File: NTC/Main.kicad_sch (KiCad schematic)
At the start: 37 parts, among them U1 TDN_5-0911WISM, X1 Barrel_Jack_Switch, X2.1 Conn_01x01_Pin, X2.2 Conn_01x01_Pin, X21 Conn_01x04_Socket, X3.1 Conn_01x01_Pin, X3.2 Conn_01x01_Pin, X4.1 Conn_01x01_Pin, X4.2 Conn_01x01_Pin, X4.3 Conn_01x01_Pin, X5.1 Conn_01x01_Pin, X5.2 Conn_01x01_Pin, X6 Conn_02x20_Counter_Clockwise

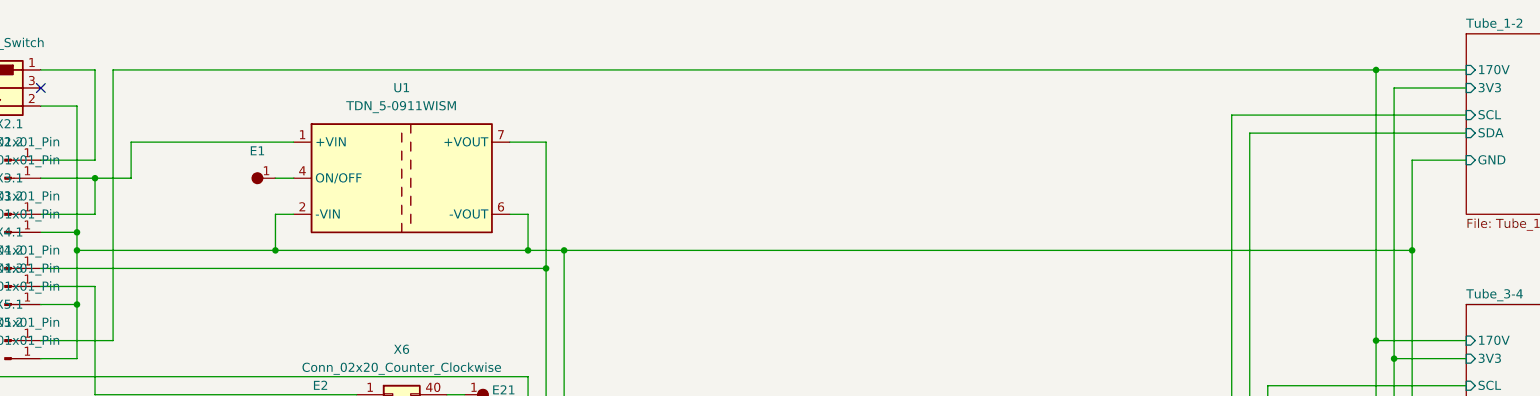
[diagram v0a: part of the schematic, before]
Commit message: Added alternative DC/DC converter and Tube schematic
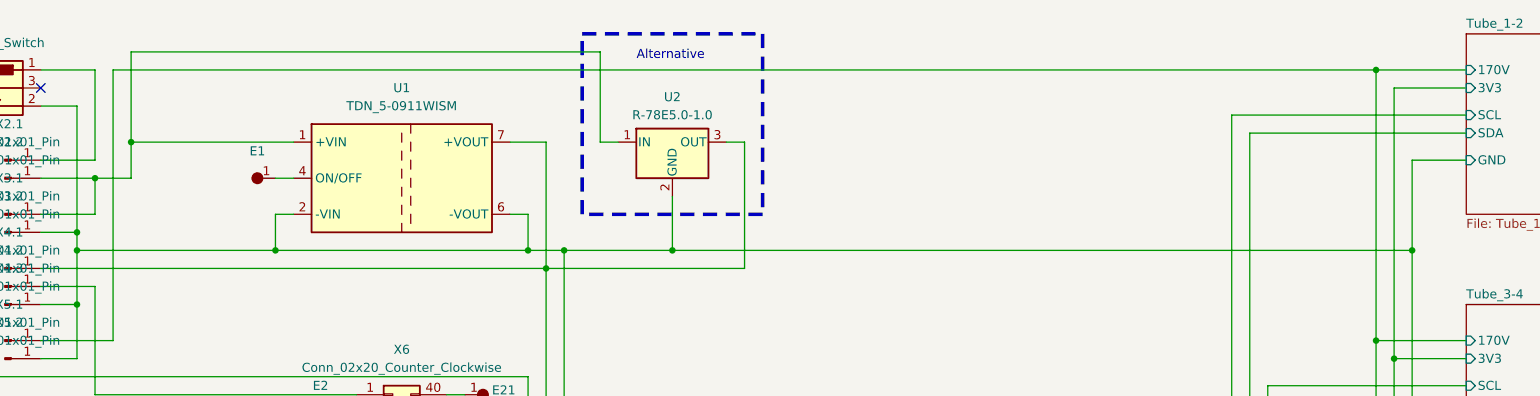
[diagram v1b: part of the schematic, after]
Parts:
- added U2: R-78E5.0-1.0, Nixie:DCDC_12V-5V-5W, symbol Regulator_Switching:R-78E5.0-1.0
- U1: footprint Converter_DCDC:Converter_DCDC_TRACO_TDN_5-xxxxWISM_SMD -> Nixie:DCDC_12V-5V-3W
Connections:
- net Tube_1-2/GND: now also U2.2 (GND)
- net at U1.1 (+VIN), X2.2.1 (Pin_1), X3.1.1 (Pin_1): now also U2.1 (IN)
- net at U1.7 (+VOUT), X4.1.1 (Pin_1), X6.39 (Pin_39): now also U2.3 (OUT)
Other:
- note added: "Alternative"
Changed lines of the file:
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@@
+	)
+	(junction
+		(at 116.84 55.88)
+		(diameter 0)
+		(color 0 0 0 0)
 	)
 	(junction
@@
 	)
 	(junction
+		(at 40.64 40.64)
+		(diameter 0)
+		(color 0 0 0 0)
+	)
+	(junction
 		(at 33.02 53.34)
 		(diameter 0)
@@
 	(wire
 		(pts
+			(xy 127 58.42) (xy 99.06 58.42)
+		)
+		(stroke
+			(width 0)
+			(type default)
+		)
+	)
+	(wire
+		(pts
+			(xy 116.84 48.26) (xy 116.84 55.88)
+		)
+		(stroke
+			(width 0)
+			(type default)
+		)
+	)
+	(wire
+		(pts
 			(xy 27.94 45.72) (xy 35.56 45.72)
 		)
@@
 	(wire
 		(pts
+			(xy 106.68 40.64) (xy 109.22 40.64)
+		)
+		(stroke
+			(width 0)
+			(type default)
+		)
+	)
+	(wire
+		(pts
 			(xy 104.14 127) (xy 104.14 124.46)
 		)
@@
 	(wire
 		(pts
+			(xy 116.84 55.88) (xy 220.98 55.88)
+		)
+		(stroke
+			(width 0)
+			(type default)
+		)
+	)
+	(wire
+		(pts
 			(xy 20.32 88.9) (xy 20.32 101.6)
 		)
@@
 	(wire
 		(pts
+			(xy 40.64 40.64) (xy 40.64 45.72)
+		)
+		(stroke
+			(width 0)
+			(type default)
+		)
+	)
+	(wire
+		(pts
 			(xy 38.1 101.6) (xy 33.02 101.6)
 		)
@@
 	(wire
 		(pts
-			(xy 101.6 55.88) (xy 220.98 55.88)
+			(xy 101.6 55.88) (xy 116.84 55.88)
 		)
 		(stroke
@@
 	(wire
 		(pts
+			(xy 106.68 27.94) (xy 106.68 40.64)
+		)
+		(stroke
+			(width 0)
+			(type default)
+		)
+	)
+	(wire
+		(pts
 			(xy 69.85 99.06) (xy 72.39 99.06)
 		)
@@
 	(wire
 		(pts
+			(xy 124.46 40.64) (xy 127 40.64)
+		)
+		(stroke
+			(width 0)
+			(type default)
+		)
+	)
+	(wire
+		(pts
 			(xy 38.1 30.48) (xy 215.9 30.48)
 		)
@@
 	(wire
 		(pts
+			(xy 127 40.64) (xy 127 58.42)
+		)
+		(stroke
+			(width 0)
+			(type default)
+		)
+	)
+	(wire
+		(pts
 			(xy 85.09 88.9) (xy 87.63 88.9)
 		)
@@
 	(wire
 		(pts
+			(xy 40.64 27.94) (xy 106.68 27.94)
+		)
+		(stroke
+			(width 0)
+			(type default)
+		)
+	)
+	(wire
+		(pts
 			(xy 27.94 63.5) (xy 33.02 63.5)
 		)
@@
 	(wire
 		(pts
-			(xy 40.64 40.64) (xy 40.64 45.72)
+			(xy 40.64 27.94) (xy 40.64 40.64)
 		)
 		(stroke
@@
 			(width 0)
 			(type default)
+		)
+	)
+	(rectangle
+		(start 104.14 25.4)
+		(end 129.54 50.8)
+		(stroke
+			(width 0.5)
+			(type dash)
+		)
+		(fill
+			(type none)
+		)
+	)
+	(text "Alternative"
+		(exclude_from_sim no)
+		(at 116.586 28.448 0)
+		(effects
+			(font
+				(size 1.27 1.27)
+			)
 		)
 	)
@@
 	)
 	(symbol
+		(lib_id "Regulator_Switching:R-78E5.0-1.0")
+		(at 116.84 40.64 0)
+		(unit 1)
+		(exclude_from_sim no)
+		(in_bom yes)
+		(on_board yes)
+		(dnp no)
+		(fields_autoplaced yes)
+		(property "Reference" "U2"
+			(at 116.84 34.29 0)
+			(effects
+				(font
+					(size 1.27 1.27)
+				)
+			)
+		)
+		(property "Value" "R-78E5.0-1.0"
+			(at 116.84 36.83 0)
+			(effects
+				(font
+					(size 1.27 1.27)
+				)
+			)
+		)
+		(property "Footprint" "Nixie:DCDC_12V-5V-5W"
+			(at 118.11 46.99 0)
+			(effects
+				(font
+					(size 1.27 1.27)
+					(italic yes)
+				)
+				(justify left)
+				(hide yes)
+			)
+		)
+		(property "Datasheet" "https://www.recom-power.com/pdf/Innoline/R-78Exx-1.0.pdf"
+			(at 116.84 40.64 0)
+			(effects
+				(font
+					(size 1.27 1.27)
+				)
+				(hide yes)
+			)
+		)
+		(property "Description" "1A Step-Down DC/DC-Regulator, 7-28V input, 5V fixed Output Voltage, LM78xx replacement, -40°C to +85°C, SIP3"
+			(at 116.84 40.64 0)
+			(effects
+				(font
+					(size 1.27 1.27)
+				)
+				(hide yes)
+			)
+		)
+		(pin "3"
+		)
+		(pin "1"
+		)
+		(pin "2"
+		)
+		(instances
+			(project ""
+				(path "/ecf22f8e-0676-4495-9357-338c1fd23f92"
+					(reference "U2")
+					(unit 1)
+				)
+			)
+		)
+	)
+	(symbol
 		(lib_id "Connector_Generic:Conn_02x20_Counter_Clockwise")
 		(at 77.47 99.06 0)
@@
 			)
 		)
-		(property "Footprint" "Converter_DCDC:Converter_DCDC_TRACO_TDN_5-xxxxWISM_SMD"
+		(property "Footprint" "Nixie:DCDC_12V-5V-3W"
 			(at 74.93 45.72 0)
 			(effects

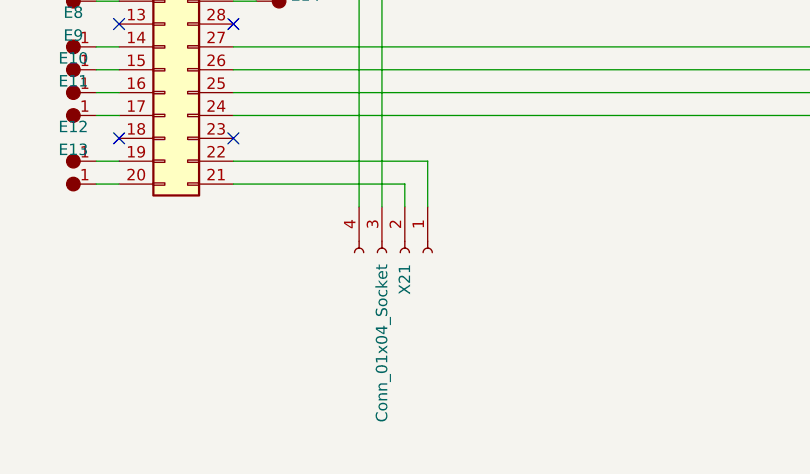
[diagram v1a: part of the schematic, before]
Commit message: Changed to 14pin socket
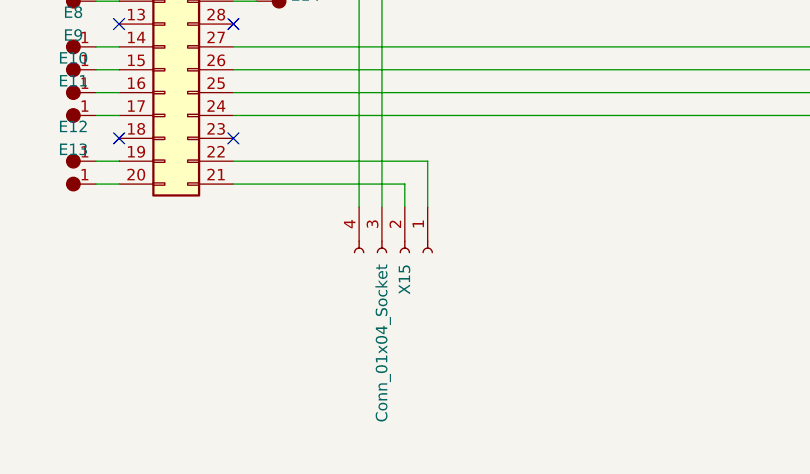
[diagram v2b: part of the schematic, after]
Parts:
- renumbered X21 to X15
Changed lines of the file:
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@@
 		(dnp no)
 		(fields_autoplaced yes)
-		(property "Reference" "X21"
+		(property "Reference" "X15"
 			(at 104.1401 133.35 0)
 			(effects
@@
 			(project ""
 				(path "/ecf22f8e-0676-4495-9357-338c1fd23f92"
-					(reference "X21")
+					(reference "X15")
 					(unit 1)
 				)

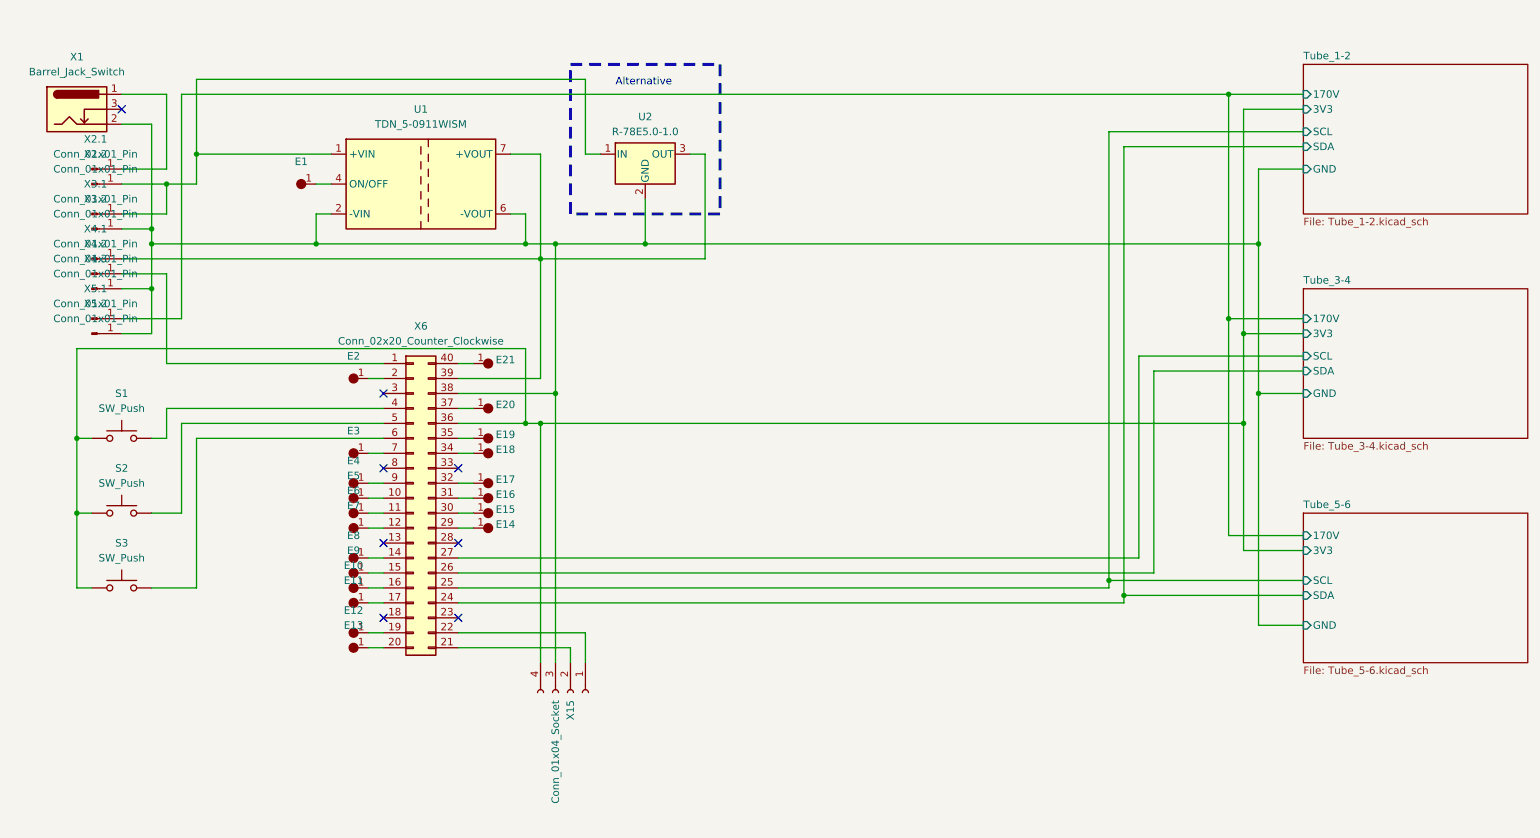
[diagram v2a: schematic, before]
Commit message: Added GPS
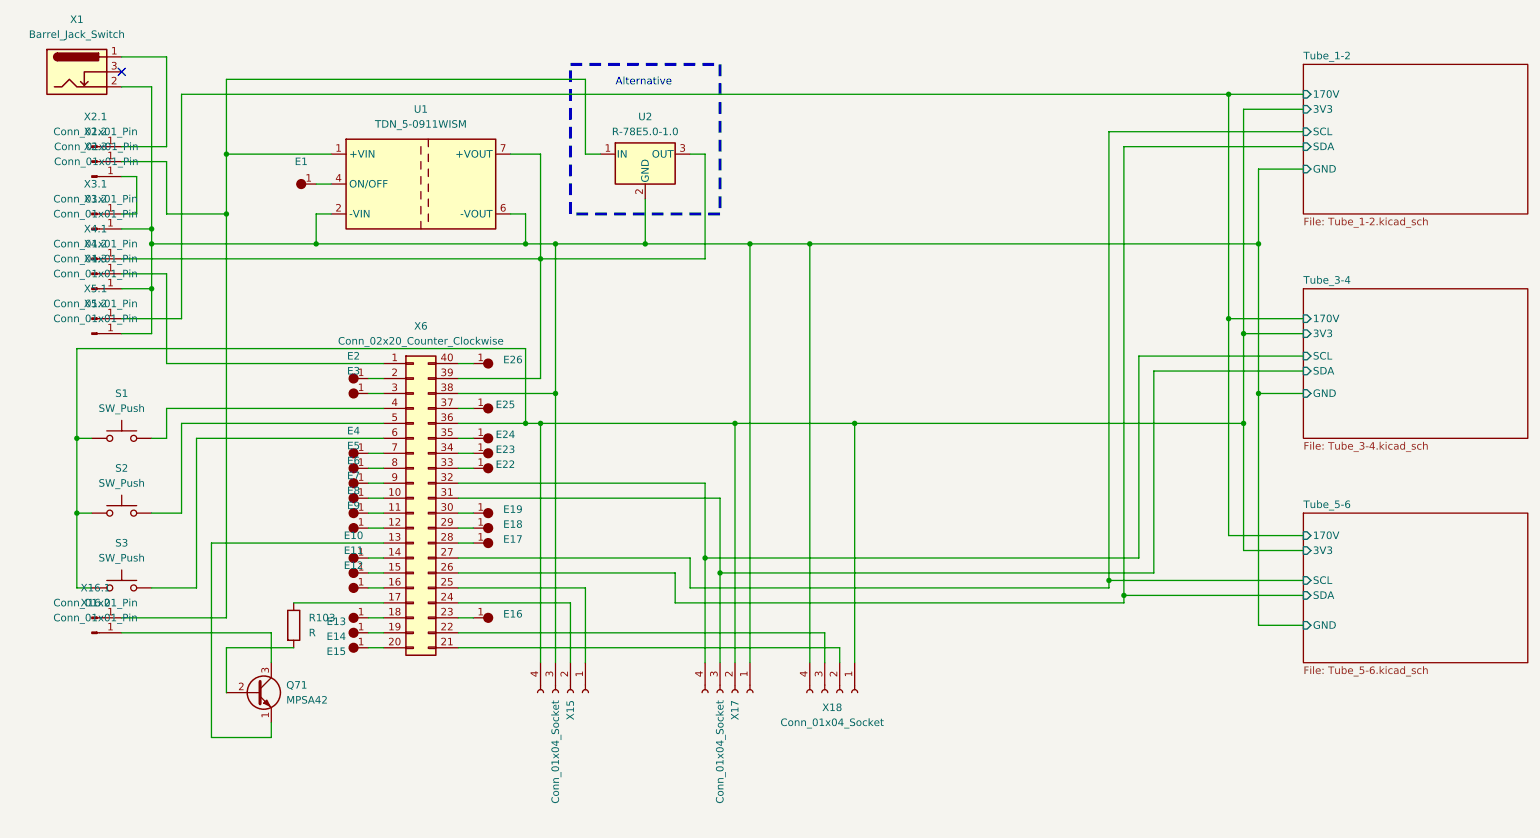
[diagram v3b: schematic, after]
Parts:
- removed E10, E14: ~, Nixie:SingleHole, symbol Nixie:Pin
- added E16, E17, E18, E19, E26: ~, Nixie:SingleHole, symbol Nixie:Pin
- added Q71: MPSA42, Nixie:MPSA-42, symbol Transistor_BJT:MPSA42
- added R103: R, Nixie:Resistor-a, symbol Device:R
- added X16.1, X16.2, X2.3: Conn_01x01_Pin, Nixie:Pin_D1.0mm_L10.0mm, symbol Connector:Conn_01x01_Pin
- added X17: Conn_01x04_Socket, Nixie:Pinbar_1-4-f-c, symbol Connector:Conn_01x04_Socket
- added X18: Conn_01x04_Socket, Nixie:Pinbar_1-4-f-d, symbol Connector:Conn_01x04_Socket
- renumbered E11 to E10, E12 to E11, E13 to E12, E15 to E13, E16 to E14, E17 to E15, E21 to E22, E20 to E23, E19 to E24, E18 to E25
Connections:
- net Tube_1-2/3V3: now also X17.2 (Pin_2), X18.1 (Pin_1)
- net Tube_1-2/GND: now also X17.1 (Pin_1), X18.4 (Pin_4)
- net Tube_1-2/SCL: now also X6.27 (Pin_27); no longer X6.25 (Pin_25)
- net Tube_1-2/SDA: now also X6.26 (Pin_26); no longer X6.24 (Pin_24)
- net Tube_3-4/SCL: now also X6.32 (Pin_32), X17.4 (Pin_4); no longer X6.27 (Pin_27)
- net Tube_3-4/SDA: now also X6.31 (Pin_31), X17.3 (Pin_3); no longer X6.26 (Pin_26)
- net at E4.1: now also X6.7 (Pin_7); no longer X6.9 (Pin_9)
- net at U1.1 (+VIN), U2.1 (IN), X2.2.1 (Pin_1): now also X16.1.1 (Pin_1); no longer X3.1.1 (Pin_1)
- net at E14.1: now also X6.19 (Pin_19); no longer X6.31 (Pin_31)
- net at E6.1: now also X6.9 (Pin_9); no longer X6.11 (Pin_11)
- net at E7.1: now also X6.10 (Pin_10); no longer X6.12 (Pin_12)
- net at E5.1: now also X6.8 (Pin_8); no longer X6.10 (Pin_10)
- net at X6.13 (Pin_13): now also Q71.1 (E)
- net at E8.1: now also X6.11 (Pin_11); no longer X6.14 (Pin_14)
- net at E9.1: now also X6.12 (Pin_12); no longer X6.15 (Pin_15)
- net at X6.16 (Pin_16): now also E12.1
- net at E10.1: now also X6.14 (Pin_14); no longer X6.17 (Pin_17)
- net at X6.18 (Pin_18): now also E13.1
- net at E11.1: now also X6.15 (Pin_15); no longer X6.19 (Pin_19)
- net at X6.20 (Pin_20): now also E15.1; no longer E12.1
- net at X6.21 (Pin_21): now also X18.2 (Pin_2); no longer X15.2 (Pin_2)
- net at X6.22 (Pin_22): now also X18.3 (Pin_3); no longer X15.1 (Pin_1)
- net at X6.23 (Pin_23): now also E16.1
- net at X6.28 (Pin_28): now also E17.1
- net at X6.29 (Pin_29): now also E18.1
- net at X6.3 (Pin_3): now also E3.1
- net at X6.30 (Pin_30): now also E19.1; no longer E13.1
- net at X6.33 (Pin_33): now also E22.1
- net at X6.34 (Pin_34): now also E23.1; no longer E25.1
- net at X6.37 (Pin_37): now also E25.1; no longer E23.1
- net at X6.40 (Pin_40): now also E26.1; no longer E22.1
- new net: X2.3.1 (Pin_1), X3.1.1 (Pin_1)
- new net: R103.1, X6.17 (Pin_17)
- new net: X15.2 (Pin_2), X6.24 (Pin_24)
- new net: X15.1 (Pin_1), X6.25 (Pin_25)
- new net: Q71.3 (C), X16.2.1 (Pin_1)
- new net: Q71.2 (B), R103.2
- no-connect marks 8 -> 1
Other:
- moved on the sheet: E10, E11, E12, E13, E14, E15, E22, E23, E25, E3, E4, E5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

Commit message: Added GPS
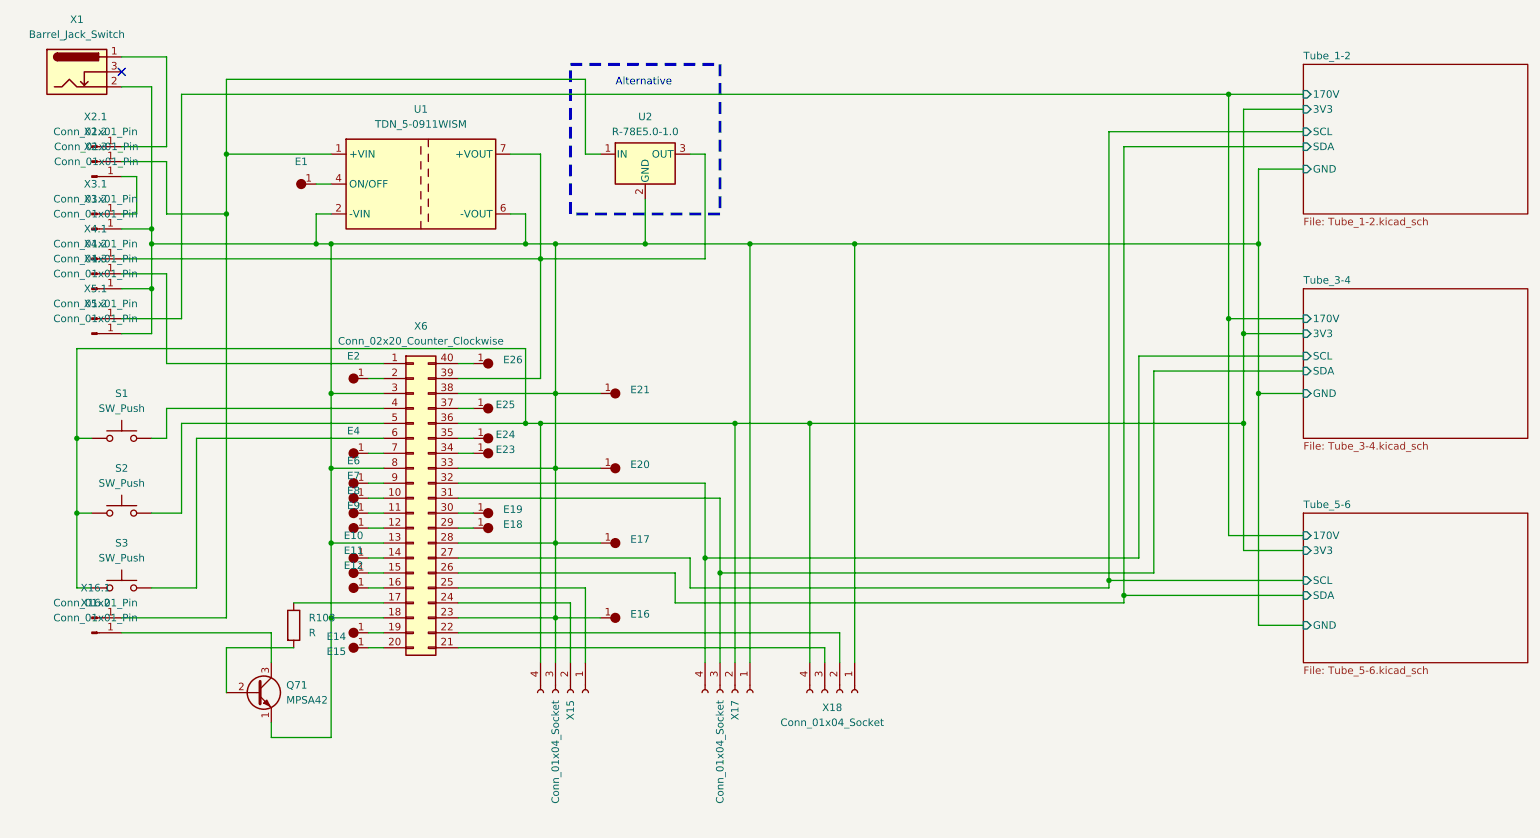
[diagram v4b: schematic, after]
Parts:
- removed E13, E22, E3, E5: ~, Nixie:SingleHole, symbol Nixie:Pin
- added E20, E21: ~, Nixie:SingleHole, symbol Nixie:Pin
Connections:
- net Tube_1-2/3V3: now also X18.4 (Pin_4); no longer X18.1 (Pin_1)
- net Tube_1-2/GND: now also E16.1, E17.1, Q71.1 (E), X18.1 (Pin_1), X6.13 (Pin_13), X6.18 (Pin_18), X6.23 (Pin_23), X6.28 (Pin_28), X6.3 (Pin_3), X6.33 (Pin_33), X6.8 (Pin_8), E20.1, E21.1; no longer X18.4 (Pin_4)
- net at X18.2 (Pin_2): now also X6.22 (Pin_22); no longer X6.21 (Pin_21)
- net at X18.3 (Pin_3): now also X6.21 (Pin_21); no longer X6.22 (Pin_22)
